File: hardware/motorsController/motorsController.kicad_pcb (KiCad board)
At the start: 2 copper layers, 166.1 x 53.6 mm, 72 parts, among them J1 batery_connector, J10 batery_connector, J11 Conn_01x04, J2 Screw_Terminal_01x01, J3 Screw_Terminal_01x01, J4 Screw_Terminal_01x01, J5 Screw_Terminal_01x01, J6 Screw_Terminal_01x01, J7 Screw_Terminal_01x01, J8 Screw_Terminal_01x01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

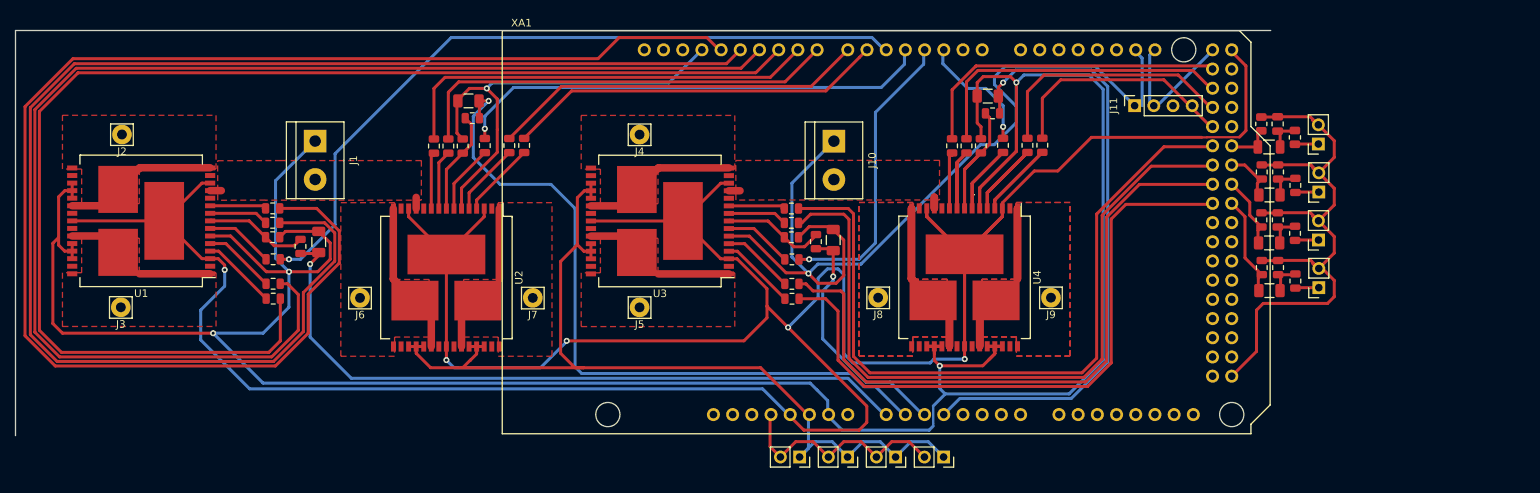
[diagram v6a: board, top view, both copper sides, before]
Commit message: fix tracks for bigger i2c connector
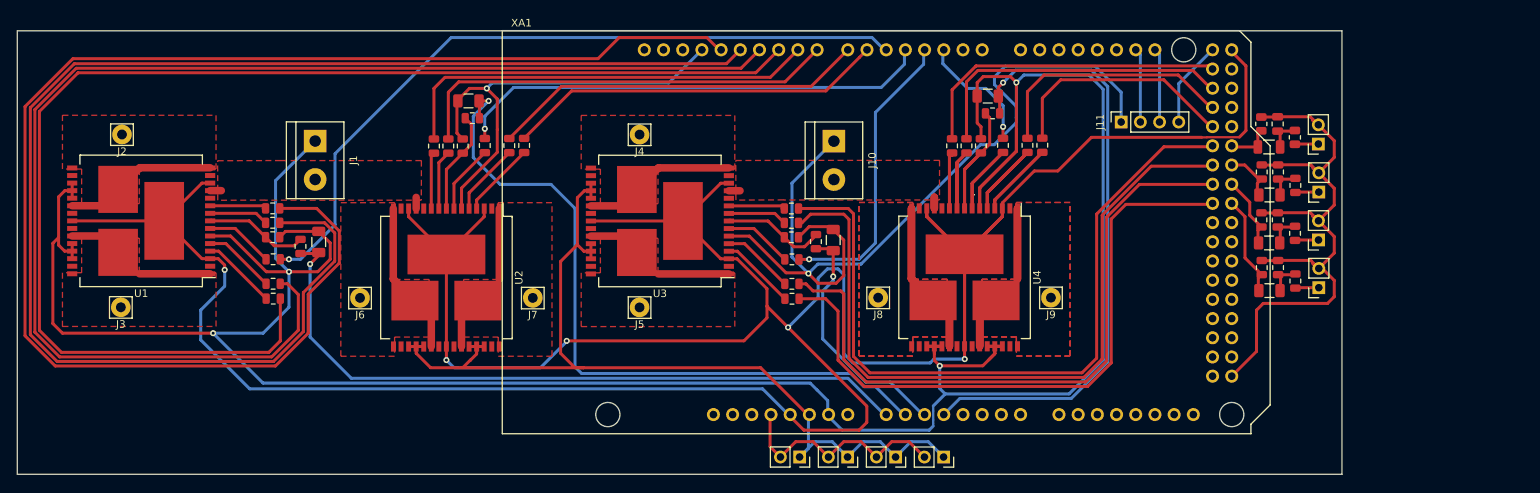
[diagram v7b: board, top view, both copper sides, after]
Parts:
- moved J11 2.80 mm to (179.2, 36.4)
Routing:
- net i2c_sda: track 7.50 -> 9.81 mm
- net i2c_scl: track 7.67 -> 9.81 mm
- net GND: track 755.0 -> 756.4 mm
- net +5V: track 427.9 -> 429.1 mm
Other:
- board size 166.1 x 53.6 mm -> 175.3 x 58.7 mm
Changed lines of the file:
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@@
   (general
     (thickness 1.6)
-    (drawings 2)
-    (tracks 677)
+    (drawings 4)
+    (tracks 679)
     (zones 0)
     (modules 72)
@@
   )
   (module Connector_PinSocket_2.54mm:PinSocket_1x04_P2.54mm_Vertical (layer F.Cu)
-    (at 180.975 34.29 90)
+    (at 179.197 36.449 90)
     (descr "Through hole straight socket strip, 1x04, 2.54mm pitch, single row (from Kicad 4.0.7), script generated")
     (tags "Through hole socket strip THT 1x04 2.54mm single row")
@@
     )
   )
-  (gr_line (start 32.90316 24.34336) (end 198.98106 24.34336) (layer Edge.Cuts) (width 0.1))
-  (gr_line (start 32.90316 77.95006) (end 32.90316 24.34336) (layer Edge.Cuts) (width 0.1))
+  (gr_line (start 208.407 24.384) (end 208.407 83.058) (layer Edge.Cuts) (width 0.1))
+  (gr_line (start 33.147 24.384) (end 208.407 24.384) (layer Edge.Cuts) (width 0.1))
+  (gr_line (start 33.147 83.058) (end 33.147 24.384) (layer Edge.Cuts) (width 0.1))
+  (gr_line (start 208.407 83.058) (end 33.147 83.058) (layer Edge.Cuts) (width 0.1))
   (segment (start 40.405 46.53) (end 40.405 44.53) (width 0.4) (layer F.Cu) (net 1))
   (segment (start 40.405 54.53) (end 40.405 52.53) (width 0.4) (layer F.Cu) (net 1))
@@
   (segment (start 162.433 30.48) (end 162.433 31.496) (width 0.4) (layer B.Cu) (net 1))
   (segment (start 162.433 31.496) (end 165.33448 34.39748) (width 0.4) (layer B.Cu) (net 1))
-  (segment (start 180.975 34.29) (end 175.75099 29.06599) (width 0.4) (layer B.Cu) (net 1))
   (segment (start 199.8605 35.7905) (end 199.898 35.753) (width 0.4) (layer F.Cu) (net 1))
   (segment (start 199.898 35.753) (end 204.22 35.753) (width 0.4) (layer F.Cu) (net 1))
@@
   (segment (start 151.384 78.74) (end 153.66238 78.74) (width 0.4) (layer B.Cu) (net 1))
   (segment (start 149.352 80.772) (end 151.384 78.74) (width 0.4) (layer B.Cu) (net 1))
+  (segment (start 179.197 32.512) (end 175.75099 29.06599) (width 0.4) (layer B.Cu) (net 1))
+  (segment (start 179.197 36.449) (end 179.197 32.512) (width 0.4) (layer B.Cu) (net 1))
   (segment (start 49.345001 42.499999) (end 58.655 42.499999) (width 1) (layer F.Cu) (net 2))
   (segment (start 46.48 45.365) (end 49.345001 42.499999) (width 1) (layer F.Cu) (net 2))
@@
   (segment (start 105.829 65.405) (end 129.286 65.405) (width 0.4) (layer F.Cu) (net 10))
   (segment (start 191.1604 27.1046) (end 191.1604 27.02306) (width 0.4) (layer B.Cu) (net 10))
-  (segment (start 183.975 34.29) (end 191.1604 27.1046) (width 0.4) (layer B.Cu) (net 10))
+  (segment (start 186.817 31.36646) (end 186.817 36.449) (width 0.4) (layer B.Cu) (net 10))
+  (segment (start 191.2874 26.89606) (end 186.817 31.36646) (width 0.4) (layer B.Cu) (net 10))
   (segment (start 72.898 53.848) (end 73.025 53.721) (width 0.4) (layer F.Cu) (net 60))
   (segment (start 70.612 53.848) (end 72.898 53.848) (width 0.4) (layer F.Cu) (net 60))
@@
   (segment (start 154.47648 47.87514) (end 154.47648 46.39614) (width 1) (layer F.Cu) (net 130))
   (segment (start 154.47648 47.87514) (end 154.47648 46.39614) (width 1) (layer F.Cu) (net 130))
-  (segment (start 182.975 27.58846) (end 182.975 34.29) (width 0.4) (layer B.Cu) (net 135))
-  (segment (start 183.5404 27.02306) (end 182.975 27.58846) (width 0.4) (layer B.Cu) (net 135))
-  (segment (start 181.975 27.99766) (end 181.975 34.29) (width 0.4) (layer B.Cu) (net 136))
-  (segment (start 181.0004 27.02306) (end 181.975 27.99766) (width 0.4) (layer B.Cu) (net 136))
+  (segment (start 184.277 27.50566) (end 183.6674 26.89606) (width 0.4) (layer B.Cu) (net 135))
+  (segment (start 184.277 36.449) (end 184.277 27.50566) (width 0.4) (layer B.Cu) (net 135))
+  (segment (start 181.737 27.50566) (end 181.1274 26.89606) (width 0.4) (layer B.Cu) (net 136))
+  (segment (start 181.737 36.449) (end 181.737 27.50566) (width 0.4) (layer B.Cu) (net 136))
   (segment (start 202.0995 37.653) (end 202.184 37.5685) (width 0.4) (layer F.Cu) (net 137))
   (segment (start 199.898 37.653) (end 202.0995 37.653) (width 0.4) (layer F.Cu) (net 137))

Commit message: layout pull-up resistors for encoders' outputs
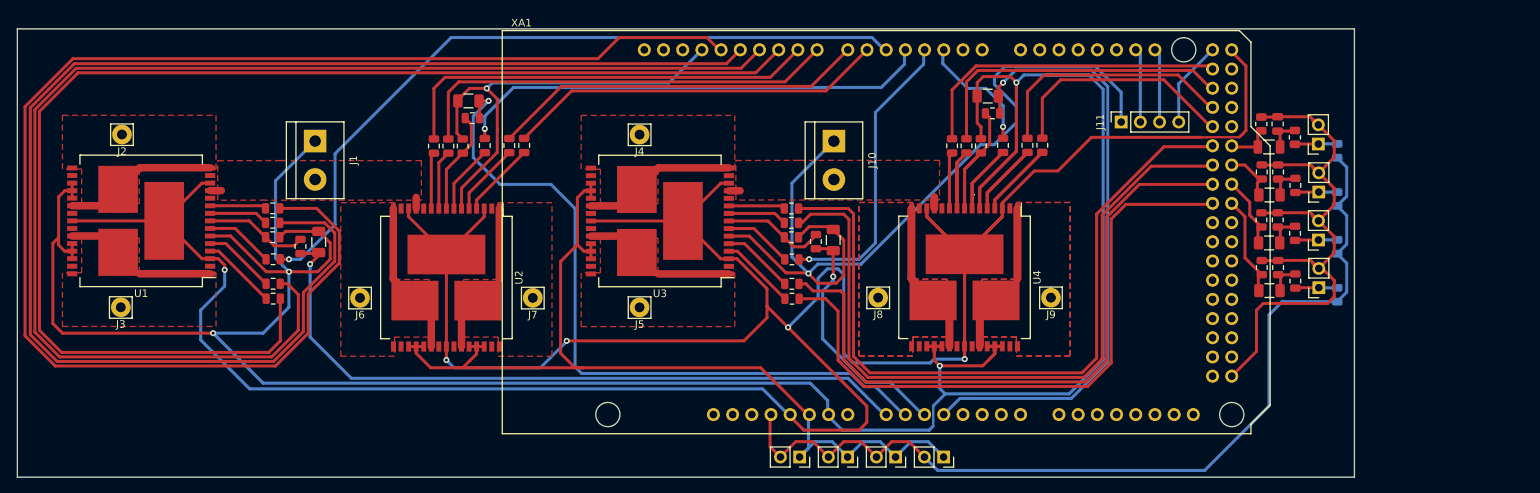
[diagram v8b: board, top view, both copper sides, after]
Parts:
- added R37: 1k, Resistor_SMD:R_0805_2012Metric, B.Cu at (207.8, 40.3)
- added R38: 1k, Resistor_SMD:R_0805_2012Metric, B.Cu at (207.8, 46.6)
- added R39: 1k, Resistor_SMD:R_0805_2012Metric, B.Cu at (207.8, 53.0)
- added R40: 1k, Resistor_SMD:R_0805_2012Metric, B.Cu at (207.8, 59.3)
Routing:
- net +3V3: track 30.2 -> 124.0 mm
- net Net-(Q1-Pad1): track 3.13 -> 5.62 mm
- net Net-(Q3-Pad1): track 3.13 -> 5.60 mm
- net Net-(Q4-Pad1): track 3.13 -> 5.57 mm
- net Net-(Q2-Pad1): track 3.13 -> 5.56 mm
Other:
- board size 175.3 x 58.7 mm -> 176.9 x 59.3 mm
